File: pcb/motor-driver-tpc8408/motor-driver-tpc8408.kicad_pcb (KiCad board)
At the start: 2 copper layers, 33 x 21 mm, 13 parts, among them J1 Conn_01x12, U1 TPC8408, U2 TPC8408, U3 74HC00

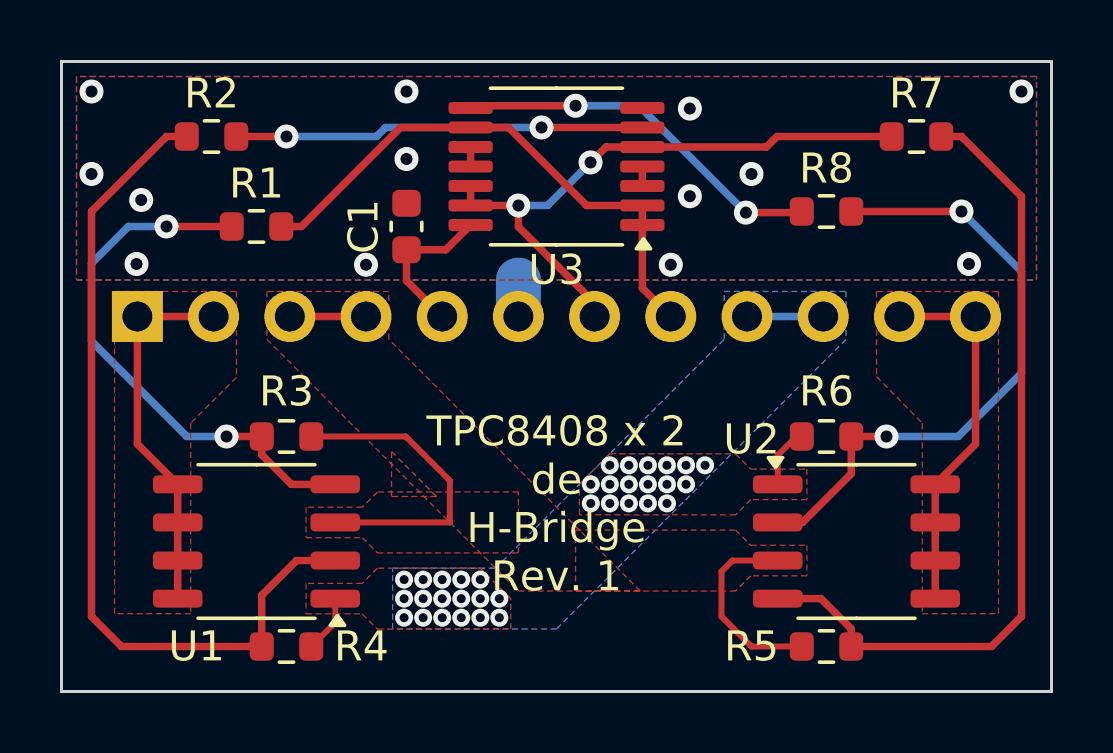
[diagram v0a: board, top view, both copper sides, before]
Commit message: 配線が間違っていたのを修正した
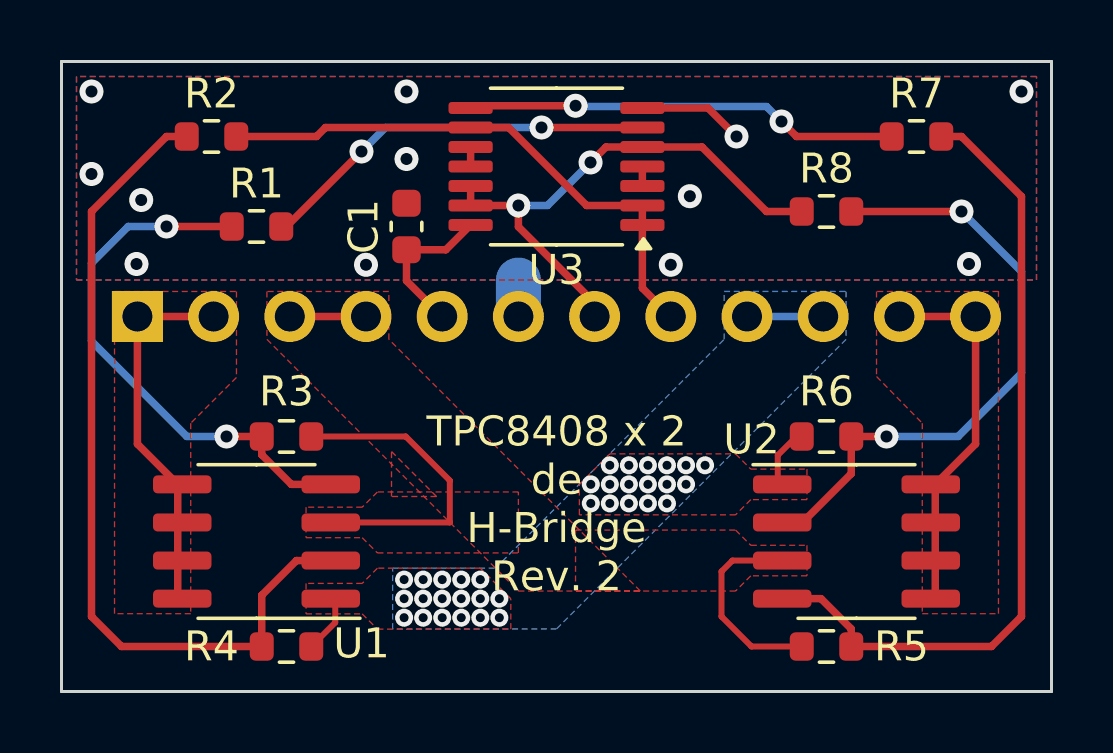
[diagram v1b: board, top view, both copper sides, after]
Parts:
- U1, U2: value TPC8408 -> FDS4559; footprint Package_SO:SOP-8_3.9x4.9mm_P1.27mm -> Package_SO:SOIC-8_3.9x4.9mm_P1.27mm
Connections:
- R1 pad 2: /IN_B -> /P1
- R2 pad 2: /P1 -> /IN_B
- R7 pad 1: /IN_A -> /P2
- R8 pad 1: /P2 -> /IN_A
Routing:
- net GND: track 1.22 -> 4.75 mm, vias 13 -> 12
- net /IN_A: track 20.4 -> 18.2 mm
- net /P2: track 12.6 -> 14.5 mm
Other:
- board text added: "@daisuke_ym 2024/09"
- board text added: "TPC8408 x 2 de H-Bridge Rev. 2"
- board text removed: "2024 Aug - @daisuke_ym"
- board text removed: "TPC8408 x 2 de H-Bridge Rev. 1"
